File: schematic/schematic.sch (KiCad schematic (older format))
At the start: 21 parts, among them J1 Conn_01x04, J19 Conn_02x05_Odd_Even, J2 Conn_01x04, J20 Conn_02x05_Odd_Even, J3 Conn_01x04, J4 Conn_01x04, J5 Conn_01x04, SW1 SW_Push_Dual, U1 STM32F401VETx, Y1 Crystal_GND24

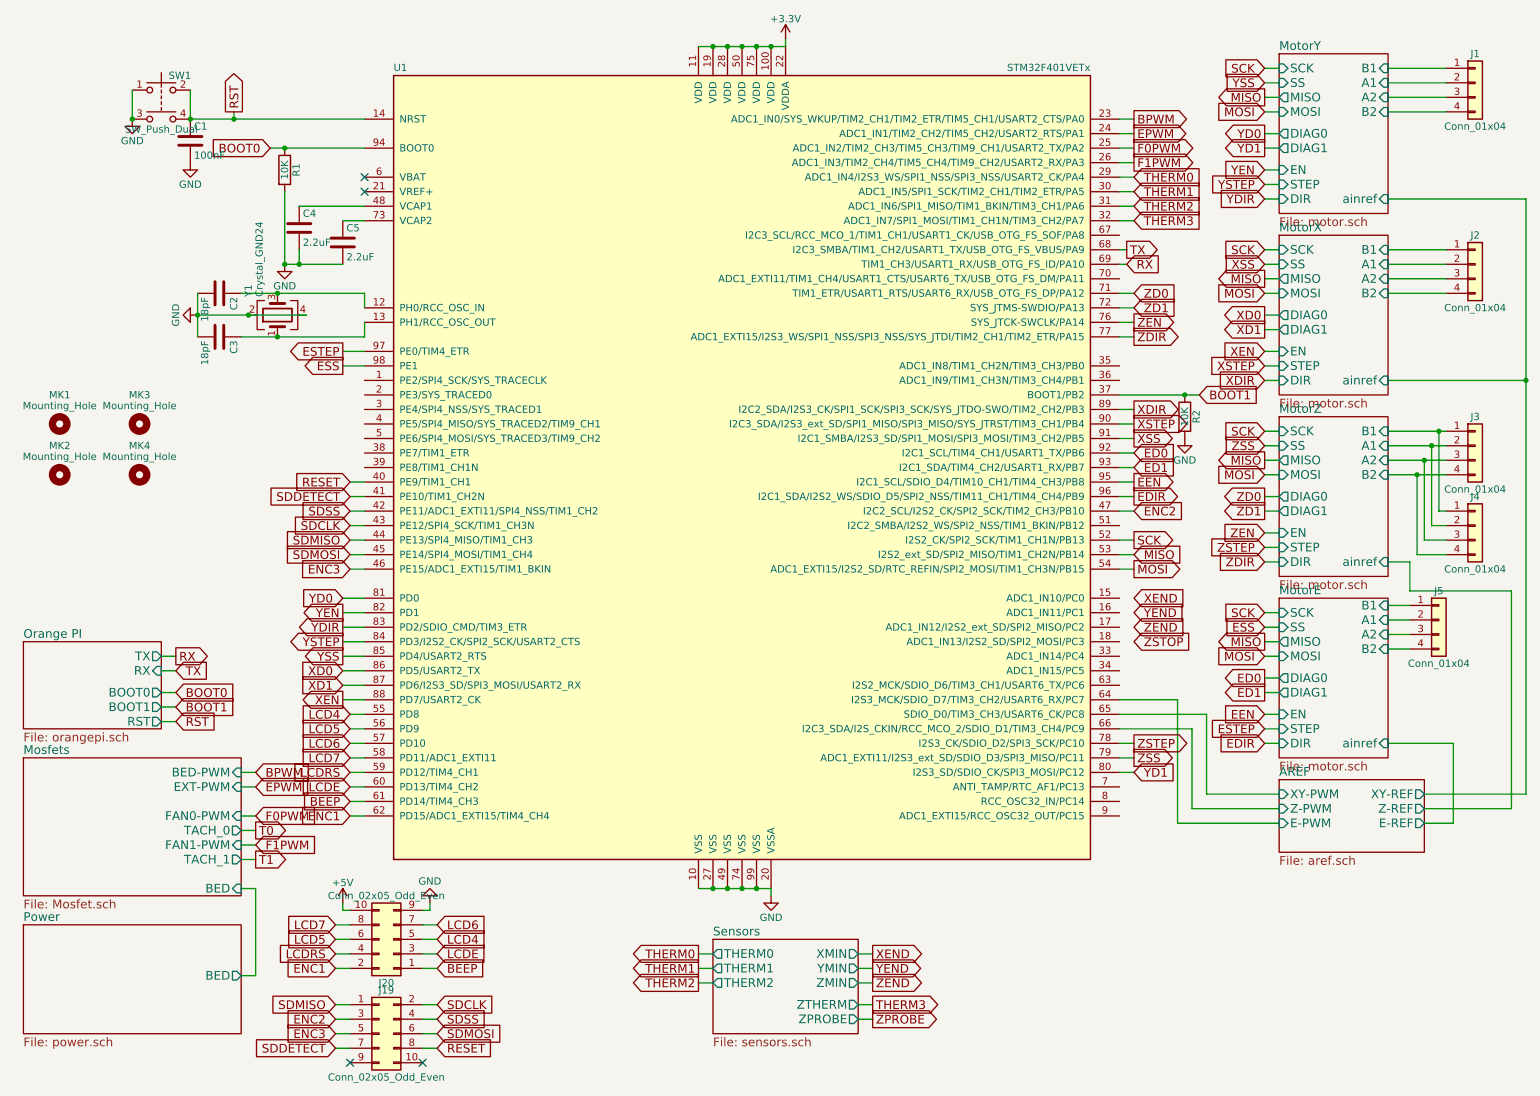
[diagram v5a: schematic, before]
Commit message: Routed signals to pi connector
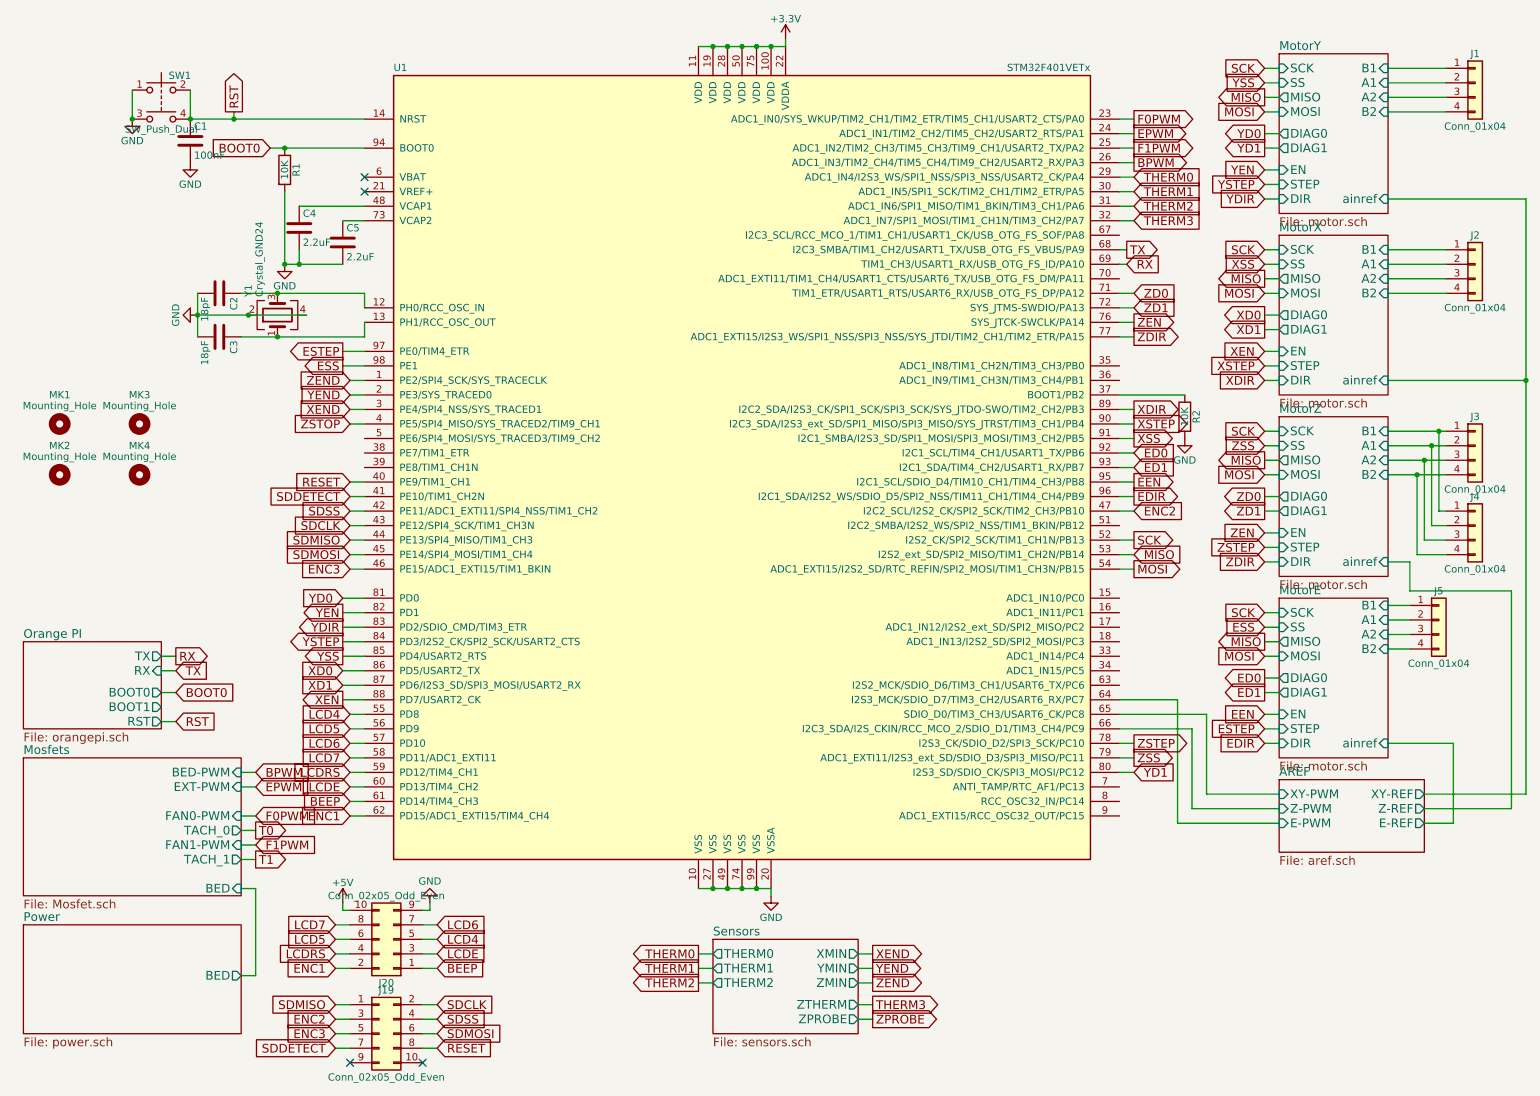
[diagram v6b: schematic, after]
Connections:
- net BPWM: now also U1.26 (ADC1_IN3/TIM2_CH4/TIM5_CH4/TIM9_CH2/USART2_RX/PA3); no longer U1.23 (ADC1_IN0/SYS_WKUP/TIM2_CH1/TIM2_ETR/TIM5_CH1/USART2_CTS/PA0)
- net F0PWM: now also U1.23 (ADC1_IN0/SYS_WKUP/TIM2_CH1/TIM2_ETR/TIM5_CH1/USART2_CTS/PA0); no longer U1.25 (ADC1_IN2/TIM2_CH3/TIM5_CH3/TIM9_CH1/USART2_TX/PA2)
- net F1PWM: now also U1.25 (ADC1_IN2/TIM2_CH3/TIM5_CH3/TIM9_CH1/USART2_TX/PA2); no longer U1.26 (ADC1_IN3/TIM2_CH4/TIM5_CH4/TIM9_CH2/USART2_RX/PA3)
- net XEND: now also U1.3 (PE4/SPI4_NSS/SYS_TRACED1)
- net YEND: now also U1.2 (PE3/SYS_TRACED0)
- net ZEND: now also U1.1 (PE2/SPI4_SCK/SYS_TRACECLK)
- net ZSTOP: now also U1.4 (PE5/SPI4_MISO/SYS_TRACED2/TIM9_CH1)
- net BOOT1: no longer names the net of R2.1, U1.37 (BOOT1/PB2)
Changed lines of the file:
@@
 	1    0    0    -1
 $EndComp
-Text GLabel 8650 3050 2    60   Input ~ 0
-BOOT1
 $Comp
 L R R2
@@
 Text GLabel 1600 5100 2    60   Input ~ 0
 BOOT0
-Text GLabel 1600 5200 2    60   Input ~ 0
-BOOT1
 Text GLabel 1600 4850 2    60   Output ~ 0
 RX
@@
 Connection ~ 2350 2150
 Wire Wire Line
-	8100 3050 8650 3050
-Connection ~ 8550 3050
-Wire Wire Line
 	1700 1150 2900 1150
 Wire Wire Line
@@
 Wire Wire Line
 	8100 2150 8150 2150
-Wire Wire Line
-	1500 5200 1600 5200
 Wire Wire Line
 	1500 5100 1600 5100
@@
 Wire Wire Line
 	2050 6250 2150 6250
-Text GLabel 8200 1150 2    60   Output ~ 0
+Text GLabel 8200 1450 2    60   Output ~ 0
 BPWM
 Text GLabel 8200 1250 2    60   Output ~ 0
 EPWM
+Text GLabel 8200 1150 2    60   Output ~ 0
+F0PWM
 Text GLabel 8200 1350 2    60   Output ~ 0
-F0PWM
-Text GLabel 8200 1450 2    60   Output ~ 0
 F1PWM
 Wire Wire Line
-	8100 1150 8200 1150
-Wire Wire Line
 	8100 1250 8200 1250
-Wire Wire Line
-	8100 1350 8200 1350
-Wire Wire Line
-	8100 1450 8200 1450
 Text GLabel 9100 800  0    60   Input ~ 0
 SCK
@@
 Wire Wire Line
 	8100 1850 8200 1850
-Text GLabel 8200 4450 2    60   Input ~ 0
+Text GLabel 2800 3150 0    60   Input ~ 0
 XEND
-Text GLabel 8200 4550 2    60   Input ~ 0
+Text GLabel 2800 3050 0    60   Input ~ 0
 YEND
-Text GLabel 8200 4650 2    60   Input ~ 0
+Text GLabel 2800 2950 0    60   Input ~ 0
 ZEND
-Text GLabel 8200 4750 2    60   Input ~ 0
+Text GLabel 2800 3250 0    60   Input ~ 0
 ZSTOP
 Text GLabel 6400 6900 2    60   Output ~ 0
@@
 Wire Wire Line
 	8700 5250 8700 5800
+Wire Wire Line
+	2800 2950 2900 2950
+Wire Wire Line
+	2800 3050 2900 3050
+Wire Wire Line
+	2800 3150 2900 3150
+Wire Wire Line
+	2800 3250 2900 3250
+Wire Wire Line
+	8100 1450 8200 1450
+Wire Wire Line
+	8100 1350 8200 1350
+Wire Wire Line
+	8100 1150 8200 1150
+Wire Wire Line
+	8100 3050 8550 3050
 $EndSCHEMATC

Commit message: Added GPIO header
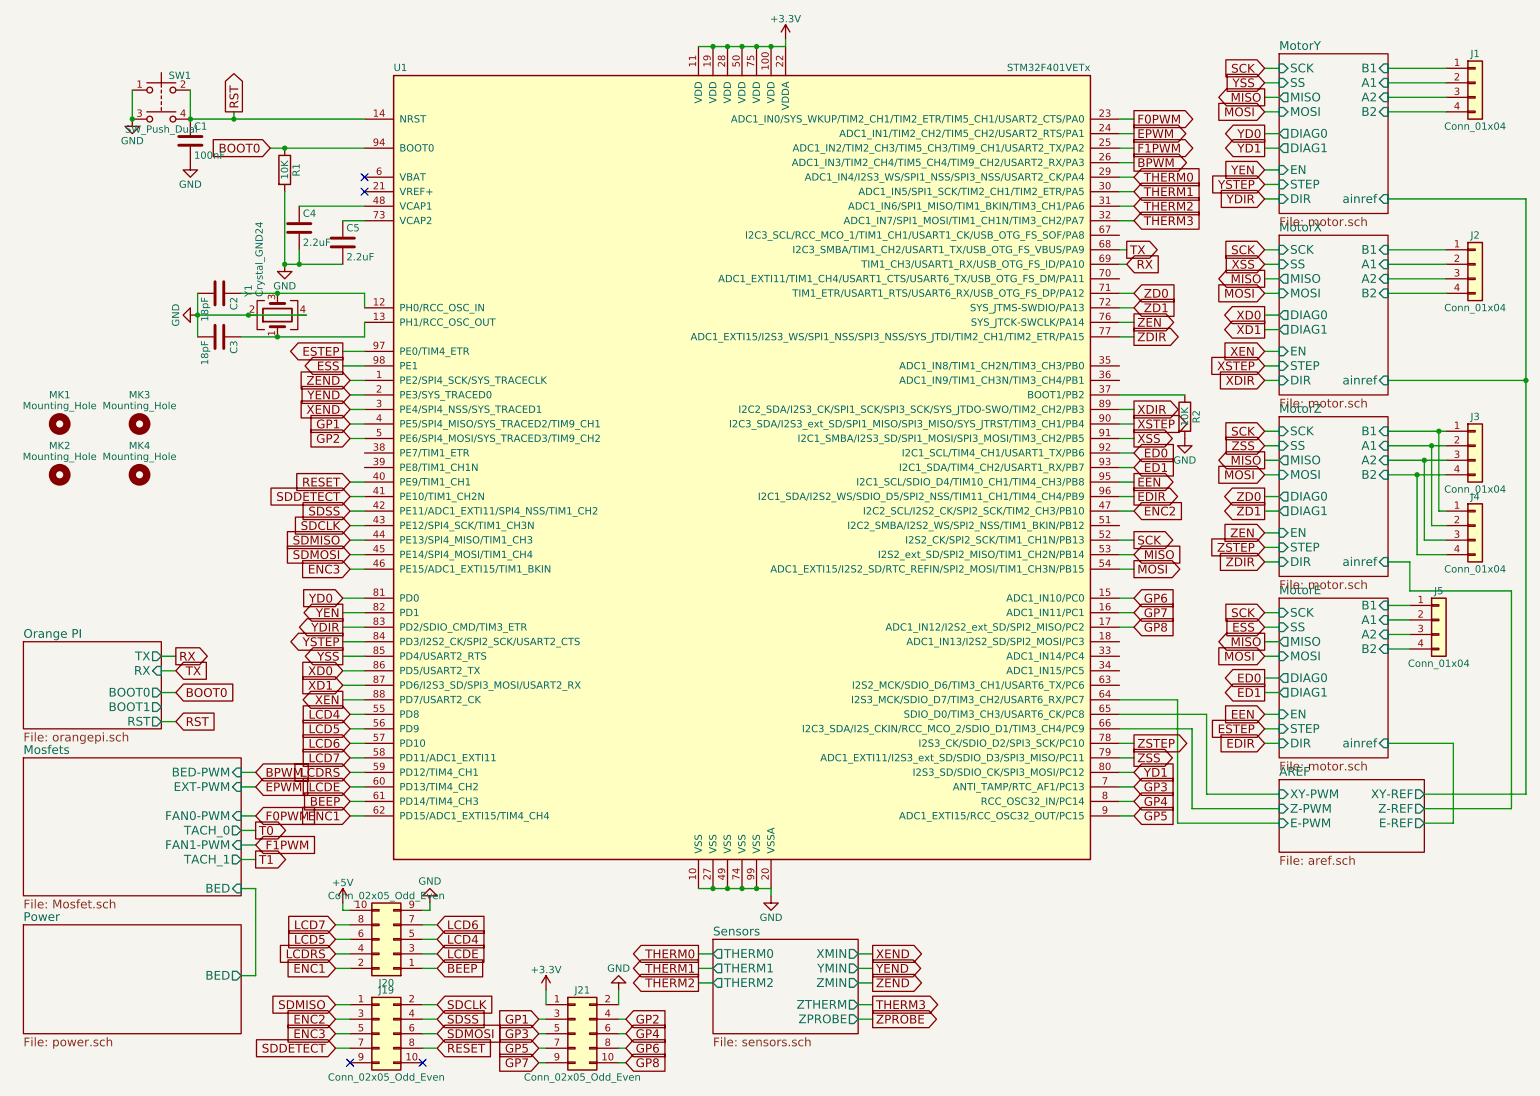
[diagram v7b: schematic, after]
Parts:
- added J21: Conn_02x05_Odd_Even, Pin_Headers:Pin_Header_Straight_2x05_Pitch2.54mm, symbol Conn_02x05_Odd_Even
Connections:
- net +3V3: now also J21.1 (Pin_1)
- net GND: now also J21.2 (Pin_2)
- net GP6: now reaches U1.15 (ADC1_IN10/PC0)
- net GP6: now also J21.8 (Pin_8)
- net GP7: now reaches U1.16 (ADC1_IN11/PC1)
- net GP7: now also J21.9 (Pin_9)
- net GP8: now reaches U1.17 (ADC1_IN12/I2S2_ext_SD/SPI2_MISO/PC2)
- net GP8: now also J21.10 (Pin_10)
- net GP2: now reaches U1.5 (PE6/SPI4_MOSI/SYS_TRACED3/TIM9_CH2)
- net GP2: now also J21.4 (Pin_4)
- net GP3: now reaches U1.7 (ANTI_TAMP/RTC_AF1/PC13)
- net GP3: now also J21.5 (Pin_5)
- net GP4: now reaches U1.8 (RCC_OSC32_IN/PC14)
- net GP4: now also J21.6 (Pin_6)
- net GP5: now reaches U1.9 (ADC1_EXTI15/RCC_OSC32_OUT/PC15)
- net GP5: now also J21.7 (Pin_7)
- net ZSTOP renamed GP1
- net GP1: now also J21.3 (Pin_3)
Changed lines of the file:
@@
 Text GLabel 2800 2950 0    60   Input ~ 0
 ZEND
-Text GLabel 2800 3250 0    60   Input ~ 0
-ZSTOP
 Text GLabel 6400 6900 2    60   Output ~ 0
 XEND
@@
 	2800 3150 2900 3150
 Wire Wire Line
+	8100 1450 8200 1450
+Wire Wire Line
+	8100 1350 8200 1350
+Wire Wire Line
+	8100 1150 8200 1150
+Wire Wire Line
+	8100 3050 8550 3050
+$Comp
+L Conn_02x05_Odd_Even J21
+U 1 1 5A762BC9
+P 4350 7450
+F 0 "J21" H 4400 7750 50  0000 C CNN
+F 1 "Conn_02x05_Odd_Even" H 4400 7150 50  0000 C CNN
+F 2 "Pin_Headers:Pin_Header_Straight_2x05_Pitch2.54mm" H 4350 7450 50  0001 C CNN
+F 3 "" H 4350 7450 50  0001 C CNN
+	1    4350 7450
+	1    0    0    -1
+$EndComp
+$Comp
+L +3.3V #PWR010
+U 1 1 5A764DEA
+P 4150 7150
+F 0 "#PWR010" H 4150 7000 50  0001 C CNN
+F 1 "+3.3V" H 4150 7290 50  0000 C CNN
+F 2 "" H 4150 7150 50  0001 C CNN
+F 3 "" H 4150 7150 50  0001 C CNN
+	1    4150 7150
+	1    0    0    -1
+$EndComp
+$Comp
+L GND #PWR011
+U 1 1 5A76523A
+P 4650 7150
+F 0 "#PWR011" H 4650 6900 50  0001 C CNN
+F 1 "GND" H 4650 7000 50  0000 C CNN
+F 2 "" H 4650 7150 50  0001 C CNN
+F 3 "" H 4650 7150 50  0001 C CNN
+	1    4650 7150
+	-1   0    0    1
+$EndComp
+Wire Wire Line
+	4150 7150 4150 7250
+Wire Wire Line
+	4650 7150 4650 7250
+Text GLabel 4100 7350 0    60   Input ~ 0
+GP1
+Text GLabel 4700 7350 2    60   Input ~ 0
+GP2
+Text GLabel 4100 7450 0    60   Input ~ 0
+GP3
+Text GLabel 4100 7550 0    60   Input ~ 0
+GP5
+Text GLabel 4100 7650 0    60   Input ~ 0
+GP7
+Text GLabel 4700 7450 2    60   Input ~ 0
+GP4
+Text GLabel 4700 7550 2    60   Input ~ 0
+GP6
+Text GLabel 4700 7650 2    60   Input ~ 0
+GP8
+Wire Wire Line
+	4100 7350 4150 7350
+Wire Wire Line
+	4100 7450 4150 7450
+Wire Wire Line
+	4100 7550 4150 7550
+Wire Wire Line
+	4100 7650 4150 7650
+Wire Wire Line
+	4650 7350 4700 7350
+Wire Wire Line
+	4650 7450 4700 7450
+Wire Wire Line
+	4650 7550 4700 7550
+Wire Wire Line
+	4650 7650 4700 7650
+Text GLabel 2800 3250 0    60   Input ~ 0
+GP1
+Text GLabel 2800 3350 0    60   Input ~ 0
+GP2
+Text GLabel 8200 5750 2    60   Input ~ 0
+GP3
+Text GLabel 8200 5850 2    60   Input ~ 0
+GP4
+Text GLabel 8200 5950 2    60   Input ~ 0
+GP5
+Text GLabel 8200 4450 2    60   Input ~ 0
+GP6
+Text GLabel 8200 4550 2    60   Input ~ 0
+GP7
+Text GLabel 8200 4650 2    60   Input ~ 0
+GP8
+Wire Wire Line
+	8100 4450 8200 4450
+Wire Wire Line
+	8100 4550 8200 4550
+Wire Wire Line
+	8100 4650 8200 4650
+Wire Wire Line
+	8100 5750 8200 5750
+Wire Wire Line
+	8100 5850 8200 5850
+Wire Wire Line
+	8100 5950 8200 5950
+Wire Wire Line
 	2800 3250 2900 3250
 Wire Wire Line
-	8100 1450 8200 1450
-Wire Wire Line
-	8100 1350 8200 1350
-Wire Wire Line
-	8100 1150 8200 1150
-Wire Wire Line
-	8100 3050 8550 3050
+	2800 3350 2900 3350
 $EndSCHEMATC
